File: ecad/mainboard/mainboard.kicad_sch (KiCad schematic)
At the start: 31 parts, among them J1 Dot Matrix Side A (M), J2 Dot Matrix Side A (F), J3 Dot Matrix Side B (F), J4 Dot Matrix Side B (M), J5 ESP32C3 Super Mini Left, J6 ESP32C3 Super Mini Right, J7 IO Expander Module - Left, J8 IO Expander Module - Right, SW1 Left Button, SW2 Right Button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

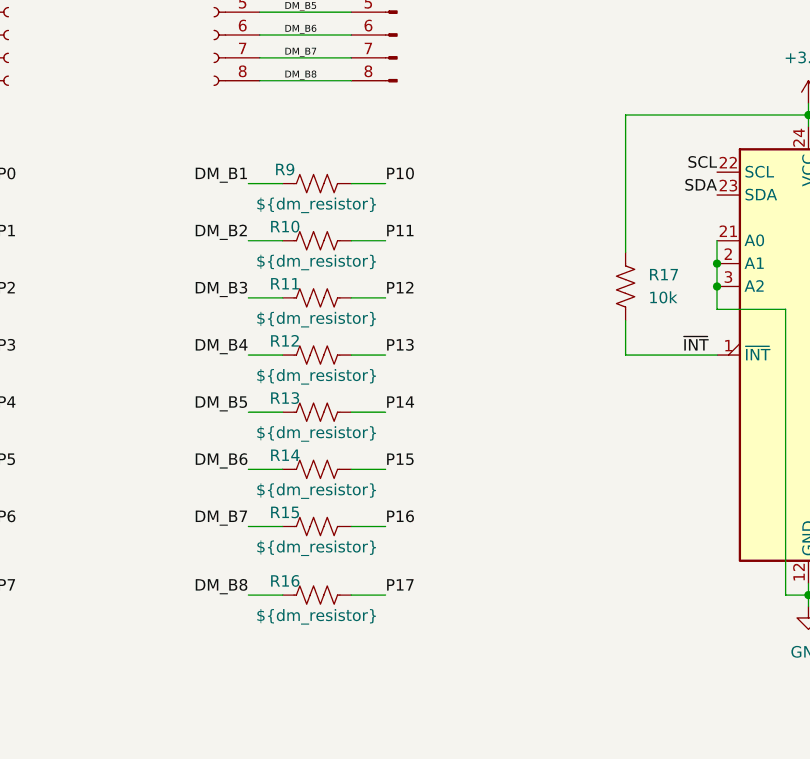
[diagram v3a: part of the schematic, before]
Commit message: place io expander (pcf8575)
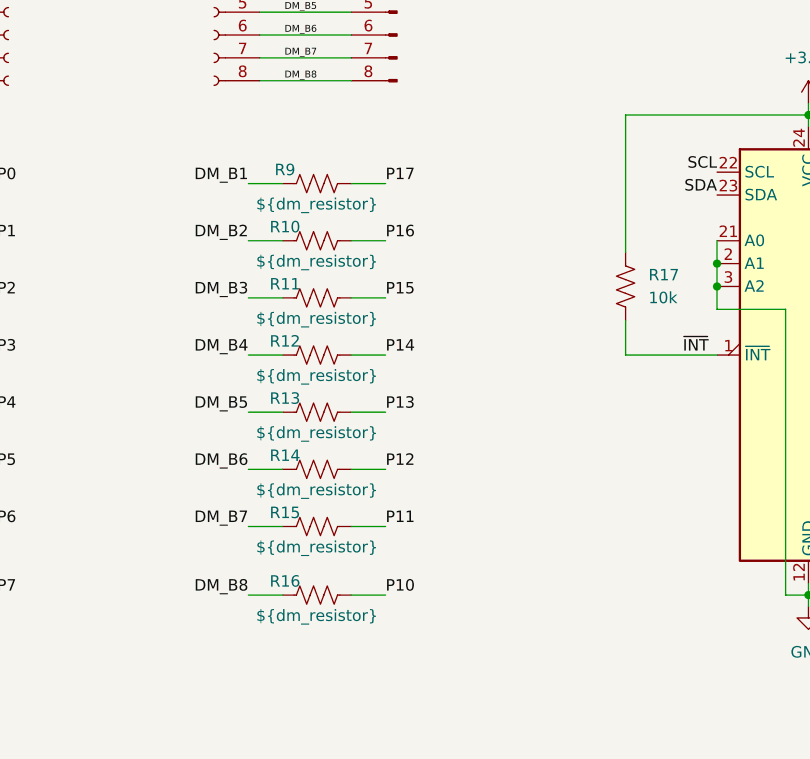
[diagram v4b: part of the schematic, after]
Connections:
- net P10: now also R16.2; no longer R9.2
- net P11: now also R15.2; no longer R10.2
- net P12: now also R14.2; no longer R11.2
- net P13: now also R13.2; no longer R12.2
- net P14: now also R12.2; no longer R13.2
- net P15: now also R11.2; no longer R14.2
- net P16: now also R10.2; no longer R15.2
- net P17: now also R9.2; no longer R16.2
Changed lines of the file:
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@@
 	)
 	(label "P10"
-		(at 151.13 96.52 0)
+		(at 151.13 142.24 0)
 		(effects
 			(font
@@
 	)
 	(label "P11"
-		(at 151.13 102.87 0)
+		(at 151.13 134.62 0)
 		(effects
 			(font
@@
 	)
 	(label "P12"
-		(at 151.13 109.22 0)
+		(at 151.13 128.27 0)
 		(effects
 			(font
@@
 	)
 	(label "P17"
-		(at 151.13 142.24 0)
+		(at 151.13 96.52 0)
 		(effects
 			(font
@@
 	)
 	(label "P15"
-		(at 151.13 128.27 0)
+		(at 151.13 109.22 0)
 		(effects
 			(font
@@
 	)
 	(label "P13"
-		(at 151.13 115.57 0)
+		(at 151.13 121.92 0)
 		(effects
 			(font
@@
 	)
 	(label "P14"
-		(at 151.13 121.92 0)
+		(at 151.13 115.57 0)
 		(effects
 			(font
@@
 	)
 	(label "P16"
-		(at 151.13 134.62 0)
-		(effects
-			(font
+		(at 151.13 102.87 0)
+		(effects
+			(font

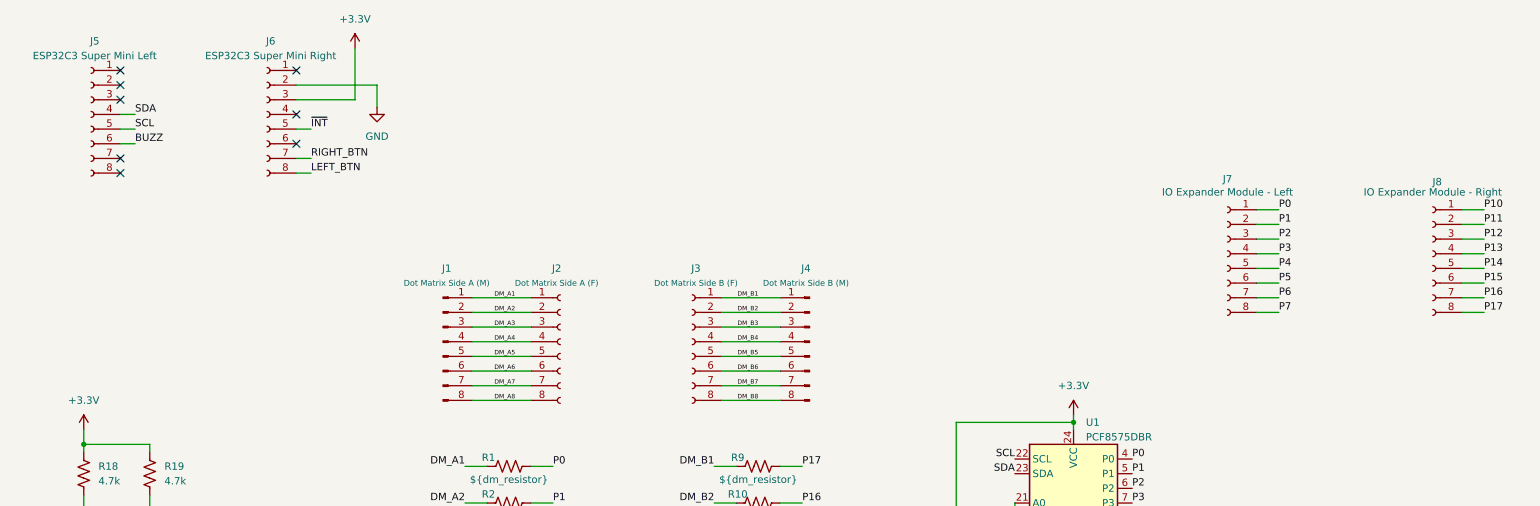
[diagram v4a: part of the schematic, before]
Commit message: remove extra pin headers for the dot matrix
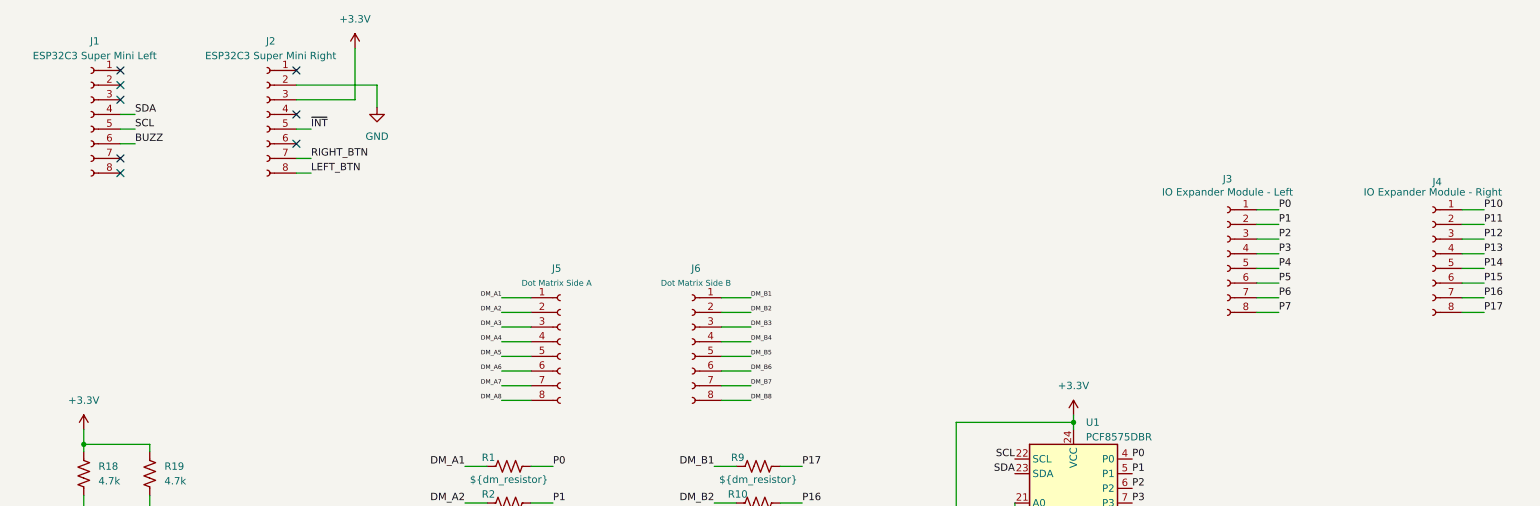
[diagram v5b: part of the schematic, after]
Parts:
- removed J1: Dot Matrix Side A (M), Connector_PinHeader_2.54mm:PinHeader_1x08_P2.54mm_Vertical, symbol Connector:Conn_01x08_Pin
- removed J4: Dot Matrix Side B (M), Connector_PinHeader_2.54mm:PinHeader_1x08_P2.54mm_Vertical, symbol Connector:Conn_01x08_Pin
- J5: renamed from J2; value Dot Matrix Side A (F) -> Dot Matrix Side A
- J6: renamed from J3; value Dot Matrix Side B (F) -> Dot Matrix Side B
- renumbered J5 to J1, J6 to J2, J7 to J3, J8 to J4

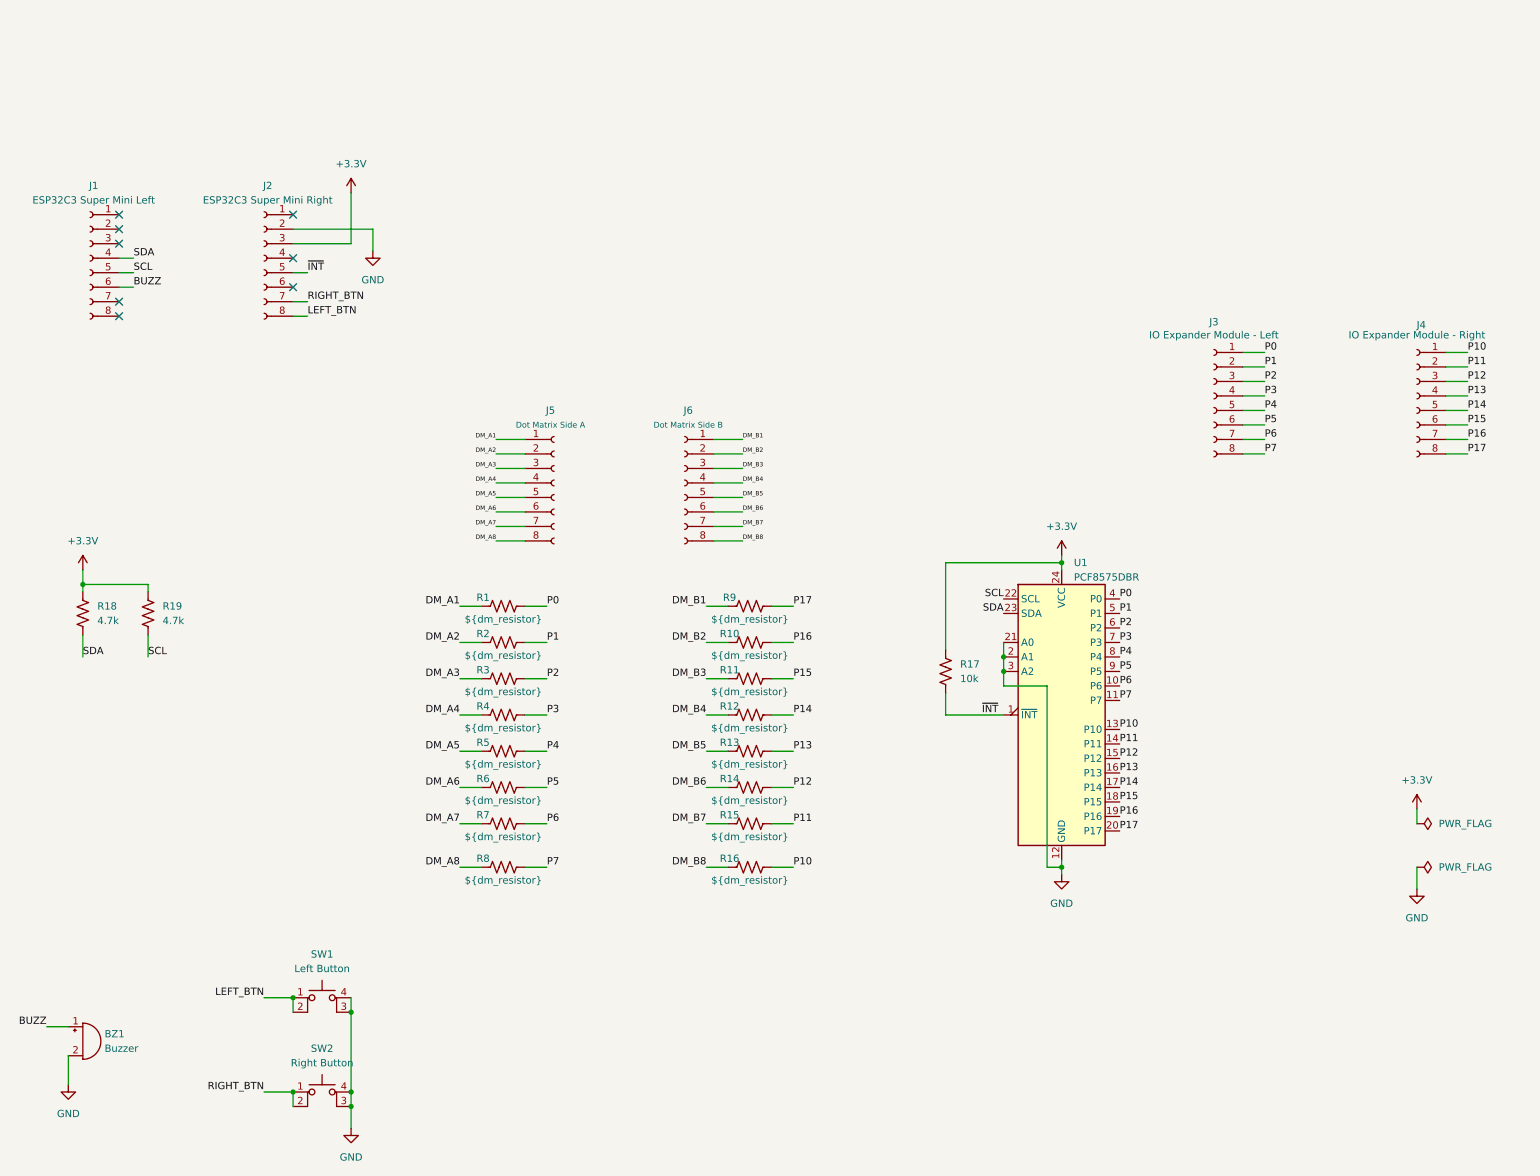
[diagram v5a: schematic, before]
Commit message: remove headers for io expander module and route tracks for the dot matrix
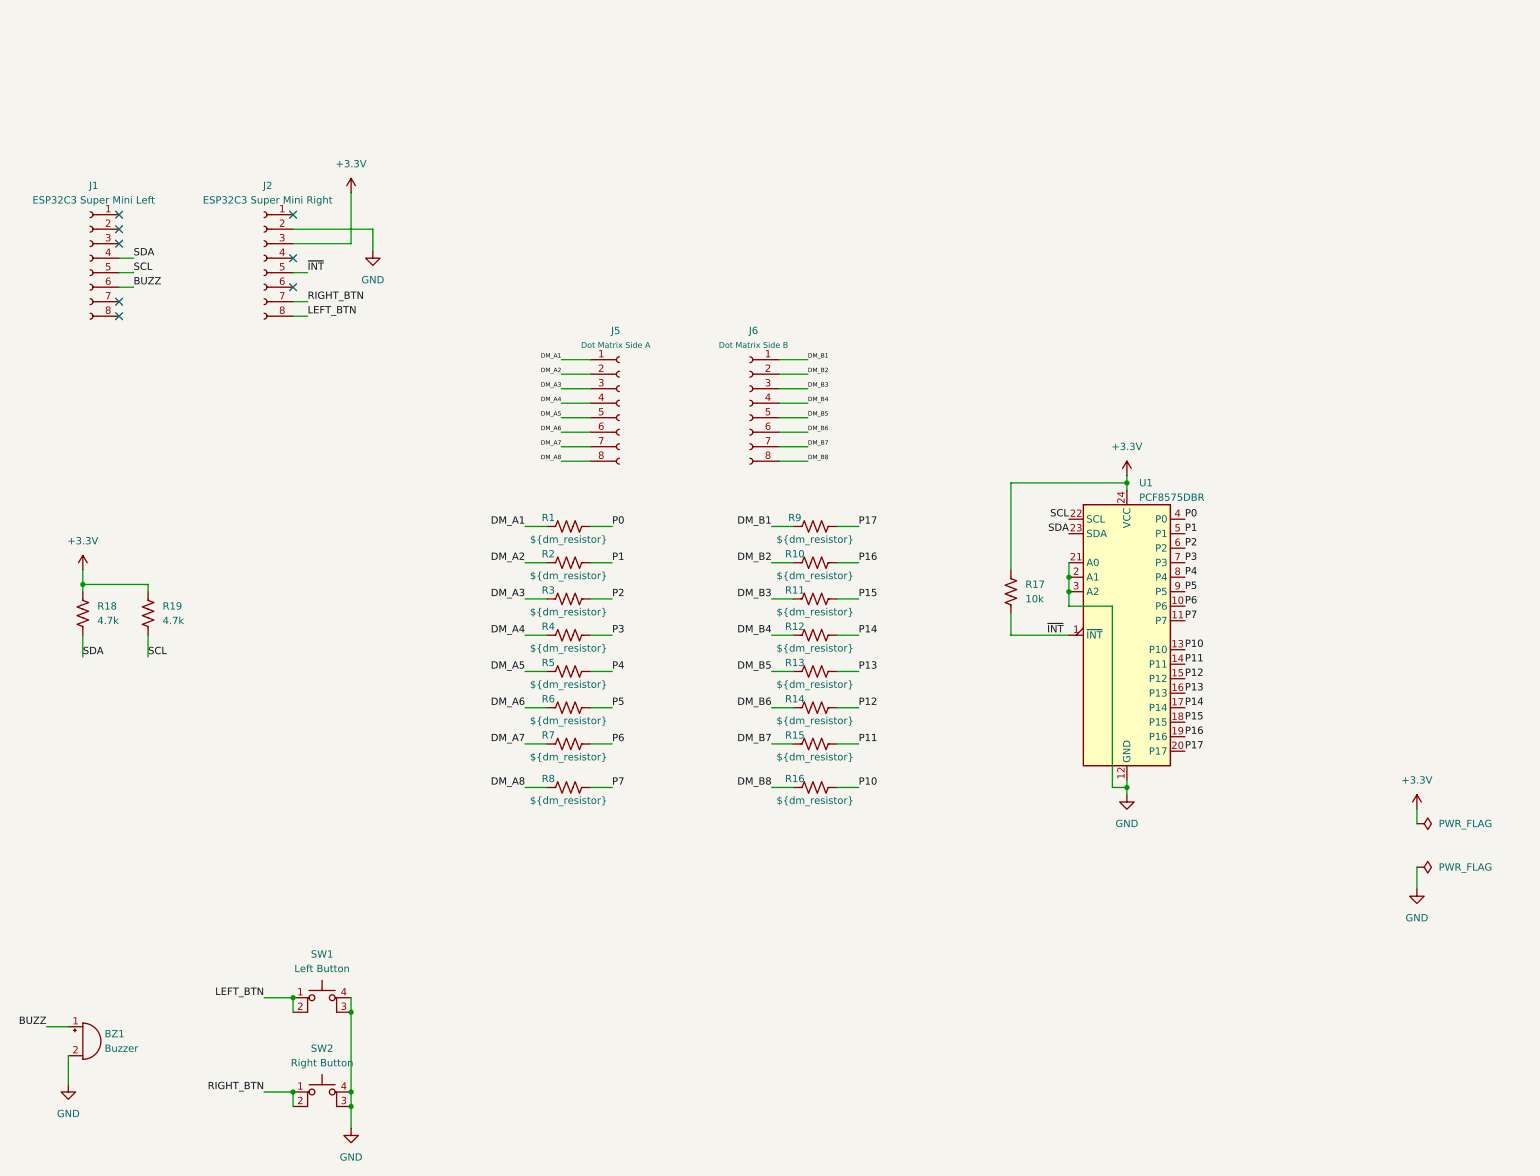
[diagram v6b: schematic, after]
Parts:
- removed J3: IO Expander Module - Left, Connector_PinSocket_2.54mm:PinSocket_1x08_P2.54mm_Vertical, symbol Connector:Conn_01x08_Socket
- removed J4: IO Expander Module - Right, Connector_PinSocket_2.54mm:PinSocket_1x08_P2.54mm_Vertical, symbol Connector:Conn_01x08_Socket
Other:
- moved on the sheet: J5, J6, R1, R10, R11, R12, R13, R14, R15, R16, R17, R2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

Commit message: add text to back silkscreen and mounting holes
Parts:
- added H1, H2, H3, H4: MountingHole, MountingHole:MountingHole_2.2mm_M2, symbol Mechanical:MountingHole
